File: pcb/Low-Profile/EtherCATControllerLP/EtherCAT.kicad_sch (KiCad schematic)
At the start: 45 parts, among them U7 LAN9252I/ML, U9 24FC512-I/SN, Y2 25 MHz, 20ppm

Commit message: checkpoint
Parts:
- C58: footprint (none) -> 0603; LCSC Part # (none) -> C106858
- FB1, FB2, FB3, FB4: LCSC Part # (none) -> C380287
- U7: footprint QFN64_ML_MCH -> (none); LCSC Part # (none) -> C2758355; LCSC Part Number C2758355 -> (none)
- U9: footprint SOIC8_4P9X3P9MC_MCH -> (none); LCSC Part # (none) -> C615159; LCSC Part Number C615159 -> (none)
- Y2: value 25 MHz, 20ppm -> ABM8-25.000MHZ-D2Y-T; LCSC Part # (none) -> C179643; LCSC Part Number C179643 -> (none)
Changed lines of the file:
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@@
 			)
 		)
-		(property "Footprint" "QFN64_ML_MCH"
+		(property "Footprint" ""
 			(at 78.74 49.53 0)
 			(effects
@@
 			)
 		)
-		(property "LCSC Part Number" "C2758355"
+		(property "LCSC Part #" "C2758355"
 			(at 78.74 49.53 0)
 			(effects
@@
 			)
 		)
-		(property "Footprint" "SOIC8_4P9X3P9MC_MCH"
+		(property "Footprint" ""
 			(at 276.86 185.42 0)
 			(effects
@@
 			)
 		)
-		(property "LCSC Part Number" "C615159"
+		(property "LCSC Part #" "C615159"
 			(at 276.86 185.42 0)
 			(effects
@@
 			)
 		)
-		(property "Value" "25 MHz, 20ppm"
-			(at 49.276 39.1159 0)
+		(property "Value" "ABM8-25.000MHZ-D2Y-T"
+			(at 40.386 39.116 0)
 			(effects
 				(font
@@
 			)
 		)
-		(property "LCSC Part Number" "C179643"
+		(property "LCSC Part #" "C179643"
 			(at 58.42 46.99 0)
 			(effects
@@
 			)
 		)
-		(property "Footprint" ""
+		(property "Footprint" "0603"
 			(at 31.75 213.36 0)
 			(effects
@@
 			)
 		)
+		(property "LCSC Part #" "C106858"
+			(at 31.75 213.36 0)
+			(effects
+				(font
+					(size 1.27 1.27)
+				)
+				(hide yes)
+			)
+		)
 		(pin "2"
 		)
@@
 			)
 		)
+		(property "LCSC Part #" "C380287"
+			(at 43.18 190.5 0)
+			(effects
+				(font
+					(size 1.27 1.27)
+				)
+				(hide yes)
+			)
+		)
 		(pin "1"
 		)
@@
 			)
 		)
+		(property "LCSC Part #" "C380287"
+			(at 43.18 162.56 0)
+			(effects
+				(font
+					(size 1.27 1.27)
+				)
+				(hide yes)
+			)
+		)
 		(pin "1"
 		)
@@
 			)
 		)
+		(property "LCSC Part #" "C380287"
+			(at 43.18 176.53 0)
+			(effects
+				(font
+					(size 1.27 1.27)
+				)
+				(hide yes)
+			)
+		)
 		(pin "1"
 		)
@@
 			(at 317.5 53.34 0)
 			(effects
+				(font
+					(size 1.27 1.27)
+				)
+				(hide yes)
+			)
+		)
+		(property "LCSC Part #" "C380287"
+			(at 317.5 53.34 0)
+			(effects

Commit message: Added XMC4800
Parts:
- removed C11, C62, C63: 0.1uF, symbol Device:C_Small
- removed C30, C31: 18pF, symbol Device:C_Small
- removed FB4: 2A, 0.05DCR, symbol Device:FerriteBead_Small
- removed R25: 4.7k, symbol Device:R_Small
- removed R26, R43: 2k, symbol Device:R_Small
- removed R7: 12.1K, symbol Device:R_Small
- removed U7: LAN9252I/ML, symbol 2024-07-01_21-03-15:LAN9252I_ML
- removed U9: 24FC512-I/SN, symbol 2024-07-03_18-39-37:24FC512-I_SN
- removed Y2: ABM8-25.000MHZ-D2Y-T, symbol Device:Crystal_GND24
- added U1, U4: KSZ8081RNA, Package_DFN_QFN:QFN-24-1EP_4x4mm_P0.5mm_EP2.6x2.6mm, symbol Interface_Ethernet:KSZ8081RNA
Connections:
- net EtherCAT3v3 renamed VCC
- new net: U4.22 (GND), U4.25 (GND)
- new net: U1.22 (GND), U1.25 (GND)
- no-connect marks 25 -> 0
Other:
- note removed: "EEPROM"
- note removed: "I2C for EEPROM"
- moved on the sheet: C32, C33, C34, C35, C36, C58, C59, C60, C61, C64, C65, C66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

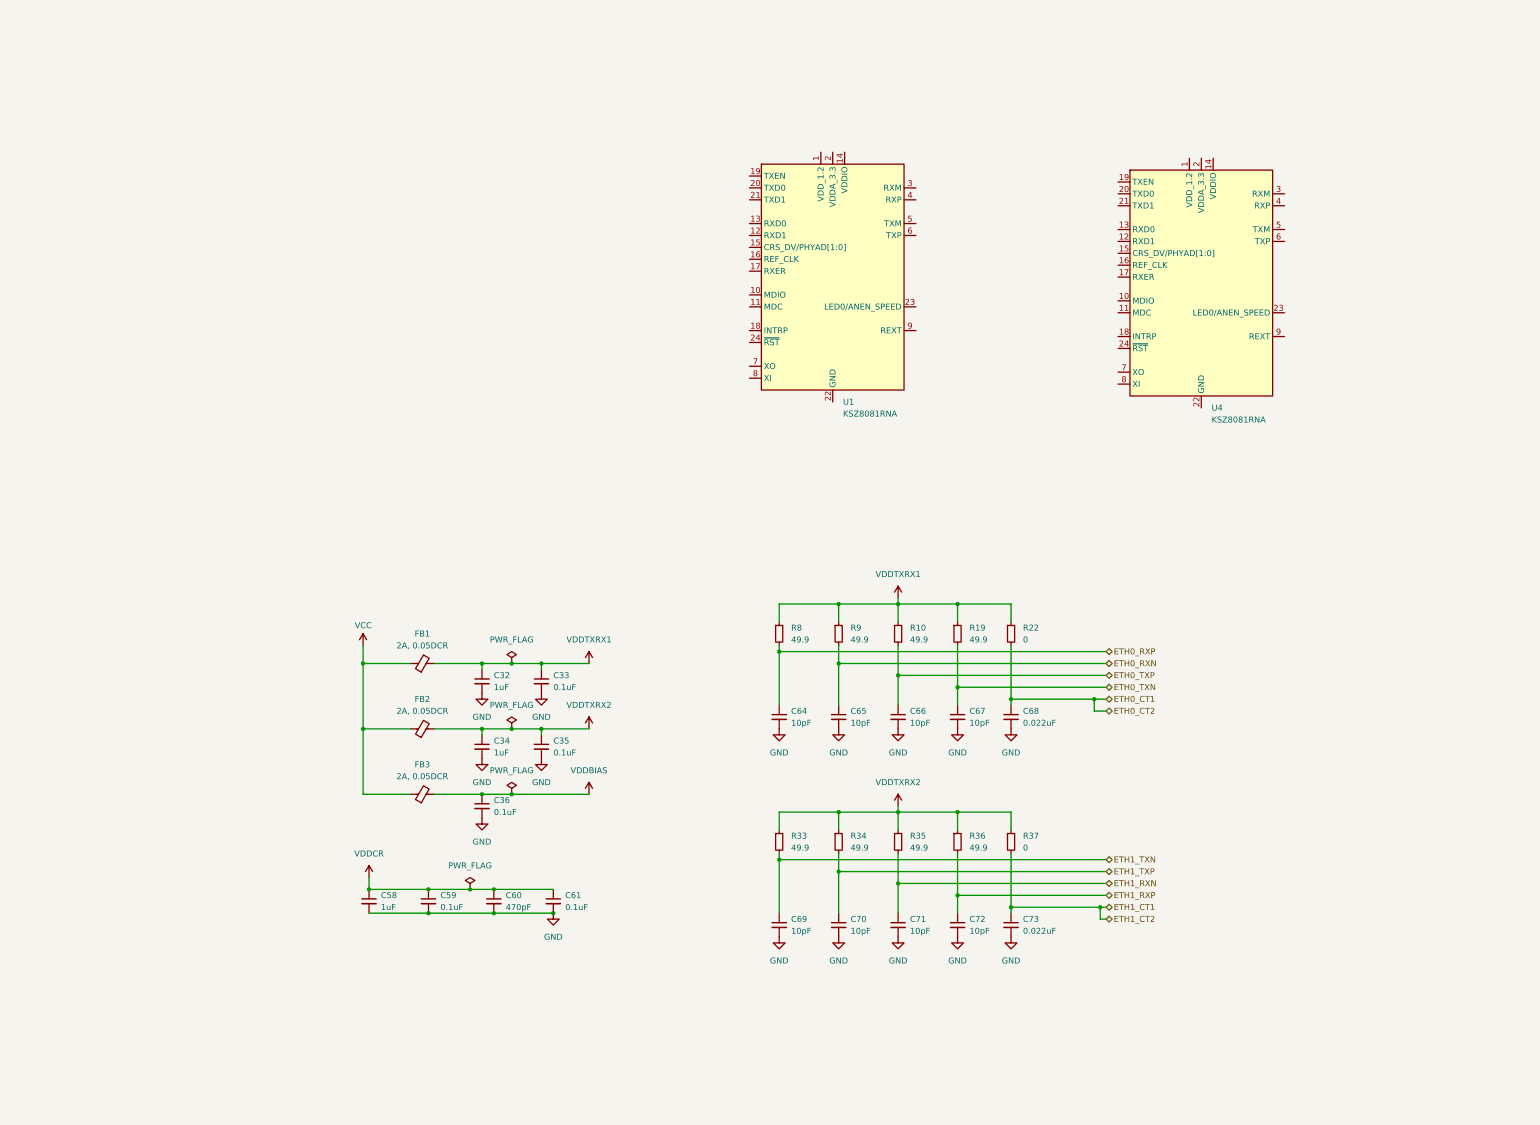
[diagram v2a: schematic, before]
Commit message: Added Ethernet PHY
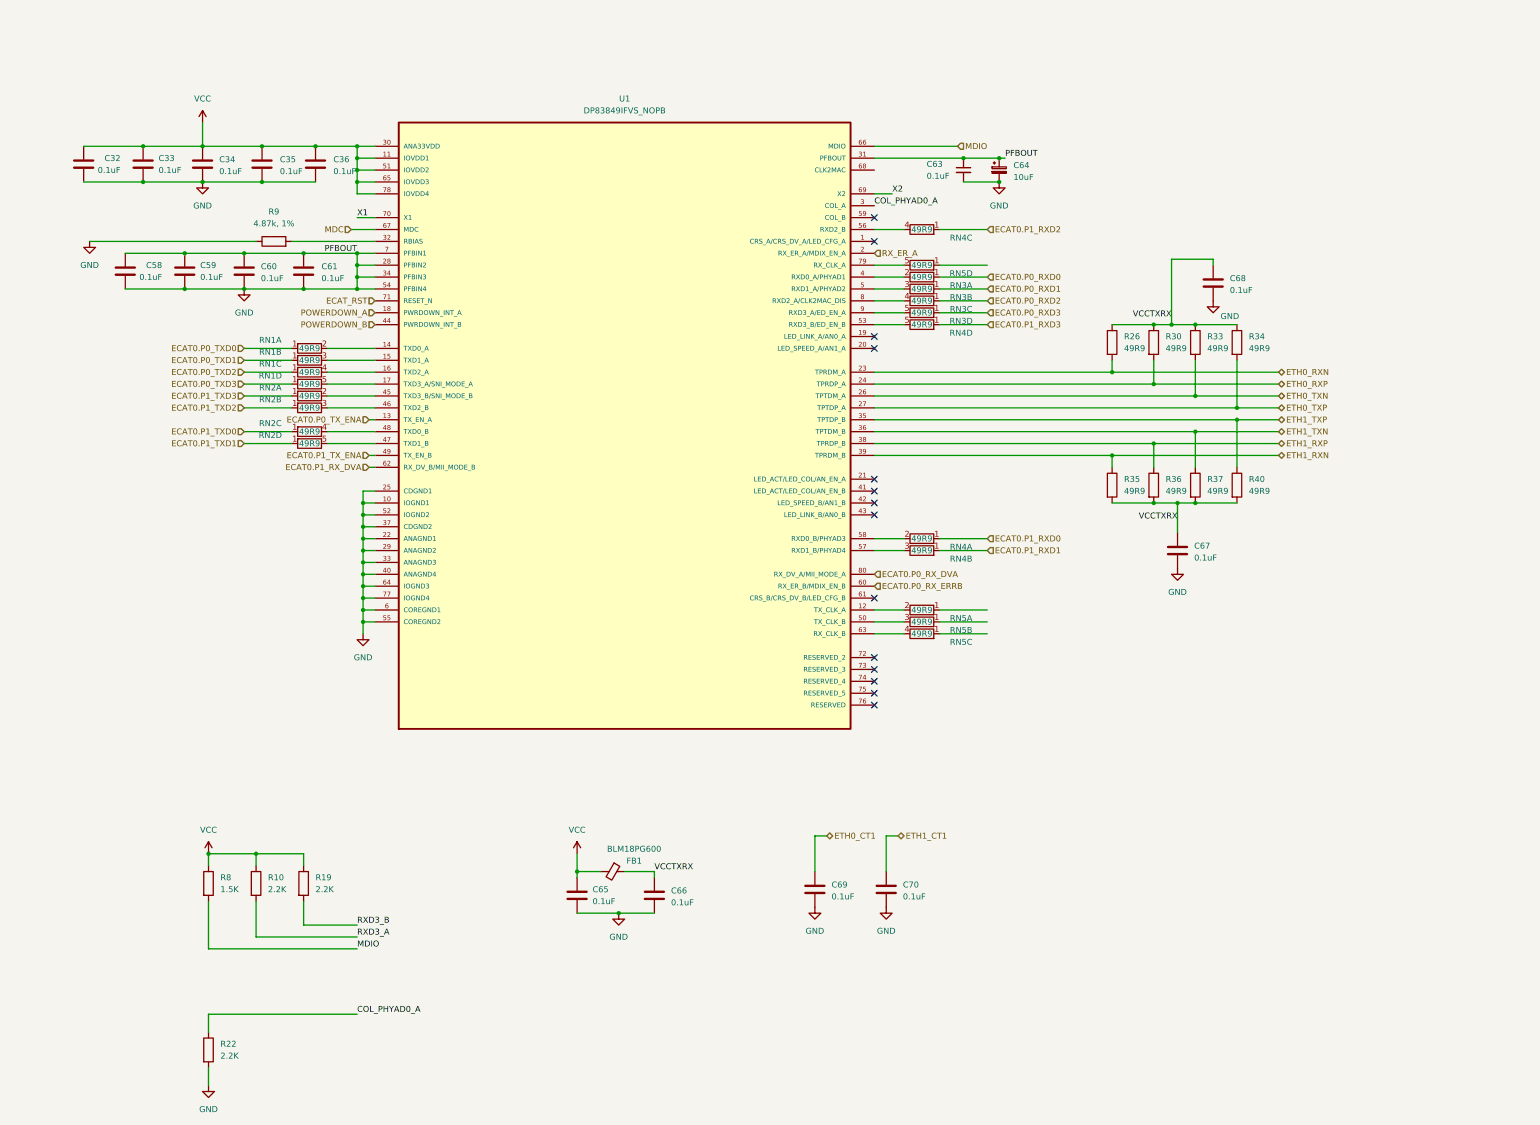
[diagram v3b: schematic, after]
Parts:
- removed C32, C34: 1uF, symbol Device:C_Small
- removed C33, C35, C36, C59, C61: 0.1uF, symbol Device:C_Small
- removed C58: 1uF, 0603, symbol Device:C_Small
- removed C60: 470pF, symbol Device:C_Small
- removed C64, C65, C66, C67, C69, C70, C71, C72: 10pF, symbol Device:C_Small
- removed C68, C73: 0.022uF, symbol Device:C_Small
- removed FB2, FB3: 2A, 0.05DCR, symbol Device:FerriteBead_Small
- removed R10, R19, R33, R34, R35, R36, R8, R9: 49.9, symbol Device:R_Small
- removed R22, R37: 0, symbol Device:R_Small
- removed U1, U4: KSZ8081RNA, Package_DFN_QFN:QFN-24-1EP_4x4mm_P0.5mm_EP2.6x2.6mm, symbol Interface_Ethernet:KSZ8081RNA
- added C32, C33, C34, C35, C36, C58, C59, C60, C61, C65, C66, C67, C68, C69, C70: ${CAPACITANCE}, Capacitor_SMD:C_0603_1608Metric, symbol Device:C
- added C63: 0.1uF, 0805, symbol Device:C_Small
- added C64: 10uF, SMD D6.3x5.4, symbol Device:C_Polarized_Small
- added R10, R19, R22: 2.2K, symbol Device:R
- added R26, R30, R33, R34, R35, R36, R37, R40: 49R9, symbol Device:R
- added R8: 1.5K, symbol Device:R
- added R9: 4.87k, 1%, symbol Device:R
- added RN1, RN2, RN3, RN4, RN5: 49R9, Resistor_THT:R_Array_SIP5, symbol Device:R_Network04_Split
- added U1: DP83849IFVS_NOPB, DP83849IFVS_NOPB:QFP50P1400X1400X120-80N, symbol DP83849IFVS_NOPB:DP83849IFVS_NOPB
- FB1: value 2A, 0.05DCR -> BLM18PG600; LCSC Part # C380287 -> C85834
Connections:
- net VDDTXRX1 is gone; now on net VCC: FB1.2
- net ETH0_CT1: now also C69.1
- net ETH0_RXN: now also R26.2, U1.23 (TPRDM_A)
- net ETH0_RXP: now also R30.2, U1.24 (TPRDP_A)
- net ETH0_TXN: now also R33.2, U1.26 (TPTDM_A)
- net ETH0_TXP: now also R34.2, U1.27 (TPTDP_A)
- net ETH1_CT1: now also C70.1
- net ETH1_RXN: now also R35.1, U1.39 (TPRDM_B)
- net ETH1_RXP: now also R36.1, U1.38 (TPRDP_B)
- net ETH1_TXN: now also R37.1, U1.36 (TPTDM_B)
- net ETH1_TXP: now also R40.1, U1.35 (TPTDP_B)
- net GND: now also C32.2, C33.2, C34.2, C35.2, C36.2, C58.1, C58.2, C59.1, C59.2, C60.1, C60.2, C61.1, C61.2, C63.1, C63.2, C64.1, C64.2, C65.2, C66.2, C67.2, C68.2, C69.2, C70.2, R22.2, R9.1, U1.10 (IOGND1), U1.22 (ANAGND1), U1.25 (CDGND1), U1.28 (PFBIN2), U1.29 (ANAGND2), U1.31 (PFBOUT), U1.33 (ANAGND3), U1.34 (PFBIN3), U1.37 (CDGND2), U1.40 (ANAGND4), U1.52 (IOGND2), U1.54 (PFBIN4), U1.55 (COREGND2), U1.6 (COREGND1), U1.64 (IOGND3), U1.7 (PFBIN1), U1.77 (IOGND4)
- net VCC: now also C32.1, C33.1, C34.1, C35.1, C36.1, C65.1, R10.1, R19.1, R8.1, U1.11 (IOVDD1), U1.30 (ANA33VDD), U1.51 (IOVDD2), U1.65 (IOVDD3), U1.78 (IOVDD4); no longer FB1.1
- new net: RN1.3 (R2.2), U1.15 (TXD1_A)
- new net: RN3.2 (R1.2), U1.4 (RXD0_A/PHYAD1)
- new net: RN1.4 (R3.2), U1.16 (TXD2_A)
- new net: RN4.4 (R3.2), U1.56 (RXD2_B)
- new net: RN2.5 (R4.2), U1.47 (TXD1_B)
- new net: RN4.3 (R2.2), U1.57 (RXD1_B/PHYAD4)
- new net: RN1.2 (R1.2), U1.14 (TXD0_A)
- new net: RN3.5 (R4.2), U1.9 (RXD3_A/ED_EN_A)
- new net: RN3.3 (R2.2), U1.5 (RXD1_A/PHYAD2)
- new net: RN2.2 (R1.2), U1.45 (TXD3_B/SNI_MODE_B)
- new net: RN5.4 (R3.2), U1.63 (RX_CLK_B)
- new net: RN5.2 (R1.2), U1.12 (TX_CLK_A)
- new net: RN1.5 (R4.2), U1.17 (TXD3_A/SNI_MODE_A)
- new net: R9.2, U1.32 (RBIAS)
- new net: RN2.3 (R2.2), U1.46 (TXD2_B)
- new net: RN2.4 (R3.2), U1.48 (TXD0_B)
- new net: RN5.3 (R2.2), U1.50 (TX_CLK_B)
- new net: RN4.5 (R4.2), U1.53 (RXD3_B/ED_EN_B)
- new net: RN4.2 (R1.2), U1.58 (RXD0_B/PHYAD3)
- new net: RN5.5 (R4.2), U1.79 (RX_CLK_A)
- new net: RN3.4 (R3.2), U1.8 (RXD2_A/CLK2MAC_DIS)
- new net COL_PHYAD0_A: R22.1, U1.3 (COL_A)
- new net ECAT0.P0_RXD0: RN3.1 (R1)
- new net ECAT0.P0_RXD1: RN3.1 (R1)
- new net ECAT0.P0_RXD2: RN3.1 (R1)
- new net ECAT0.P0_RXD3: RN3.1 (R1)
- new net ECAT0.P0_RX_DVA: U1.80 (RX_DV_A/MII_MODE_A)
- new net ECAT0.P0_RX_ERRB: U1.60 (RX_ER_B/MDIX_EN_B)
- new net ECAT0.P0_TXD0: RN1.1 (R1)
- new net ECAT0.P0_TXD1: RN1.1 (R1)
- new net ECAT0.P0_TXD2: RN1.1 (R1)
- new net ECAT0.P0_TXD3: RN1.1 (R1)
- new net ECAT0.P0_TX_ENA: U1.13 (TX_EN_A)
- new net ECAT0.P1_RXD0: RN4.1 (R1)
- new net ECAT0.P1_RXD1: RN4.1 (R1)
- new net ECAT0.P1_RXD2: RN4.1 (R1)
- new net ECAT0.P1_RXD3: RN4.1 (R1)
- new net ECAT0.P1_RX_DVA: U1.62 (RX_DV_B/MII_MODE_B)
- new net ECAT0.P1_TXD0: RN2.1 (R1)
- new net ECAT0.P1_TXD1: RN2.1 (R1)
- new net ECAT0.P1_TXD2: RN2.1 (R1)
- new net ECAT0.P1_TXD3: RN2.1 (R1)
- new net ECAT0.P1_TX_ENA: U1.49 (TX_EN_B)
- new net ECAT_RST: U1.71 (RESET_N)
- new net MDC: U1.67 (MDC)
- new net MDIO: R8.2, U1.66 (MDIO)
- new net POWERDOWN_A: U1.18 (PWRDOWN_INT_A)
- new net POWERDOWN_B: U1.44 (PWRDOWN_INT_B)
- new net RXD3_A: R10.2
- new net RXD3_B: R19.2
- new net RX_ER_A: U1.2 (RX_ER_A/MDIX_EN_A)
- new net VCCTXRX: C66.1, C67.1, C68.1, FB1.1, R26.1, R30.1, R33.1, R34.1, R35.2, R36.2, R37.2, R40.2
- new net X1: U1.70 (X1)
- new net X2: U1.69 (X2)
- no-connect marks 0 -> 14
